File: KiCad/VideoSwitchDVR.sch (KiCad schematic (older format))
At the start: 7 parts, among them SW1 Joystick, U1 ATTINY84-20MU, U2 MAX4624/5

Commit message: Some progress on PCB. MCU changed to simplier one
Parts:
- removed SW1: Joystick, KiCadCustomLibs:5dir6pin10x10mm_Joystick, symbol Joystick
- removed U1: ATTINY84-20MU, Housings_DFN_QFN:UQFN-20-1EP_4x4mm_Pitch0.5mm, symbol ATTINY84-20MU
- added C5: 22uf, Capacitors_SMD:C_0805, symbol C
- added J1: EV100, KiCadCustomLibs:USB_3_PADS, symbol Conn_01x03
- added J2: Buttons, KiCadCustomLibs:USB_3_PADS, symbol Conn_01x03
- added J3: DVR_VIDEO, KiCadCustomLibs:USB_3_PADS, symbol Conn_01x03
- added J4: PWR, KiCadCustomLibs:POWER2PIN, symbol Conn_01x02
- added J5: PWR_DVR, KiCadCustomLibs:POWER2PIN, symbol Conn_01x02
- added J6: PROG, KiCadCustomLibs:Pads_prog_6pin1.25mm, symbol Conn_01x06
- added R1, R2, R3, R4: 100, Resistors_SMD:R_0603, symbol R
- added R5: 10K, Resistors_SMD:R_0603, symbol R
- added U1: ATTINY15-1SC, Housings_SOIC:SOIJ-8_5.3x5.3mm_Pitch1.27mm, symbol ATTINY15-1SC
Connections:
- net labels added: K1, K2, K3, MISO, MOSI, RST, SCK, VID_SENSE, VID_SWITCH
- wire segments 12 -> 37
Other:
- moved on the sheet: C1, C2

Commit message: Some work
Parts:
- removed J2: Buttons, KiCadCustomLibs:USB_3_PADS, symbol Conn_01x03
- added D1: B5819WS, Diodes_SMD:D_SOD-323, symbol D_Schottky
- added J2: Buttons, KiCadCustomLibs:POWER2PIN, symbol Conn_01x02
- added JP1: VCC_SENSE, Resistors_SMD:R_0201_NoSilk, symbol Jumper_NO_Small
- added Q1: AO3415 (P), TO_SOT_Packages_SMD:SOT-23, symbol Q_PMOS_GSD
- added R6: 1K, Resistors_SMD:R_0603, symbol R
- R2: value 100 -> 100K
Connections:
- net K2 is gone; now on net VCC: R2.1
- net MISO: now also R6.1; no longer R2.2
- net VCC: now also D1.1 (K), JP1.2, Q1.2 (S); no longer C5.1, J4.1 (Pin_1), J5.1 (Pin_1)
- net VID_SWITCH: now also U2.1 (IN); no longer U2.5 (COM)
- net at J1.1 (Pin_1): now also U2.5 (COM); no longer U2.1 (IN)
- net K1 renamed B0
- net B0: now also J2.2 (Pin_2), JP1.1
- net K3 renamed B2
- net B2: now also J2.1 (Pin_1)
- new net: D1.2 (A), J4.1 (Pin_1)
- new net: C5.1, J5.1 (Pin_1), Q1.3 (D)
- new net: Q1.1 (G), R2.2, R6.2
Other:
- moved on the sheet: C1, C2, C3, C4, C5, J1, J3, J4, J5, J6, R1, R3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

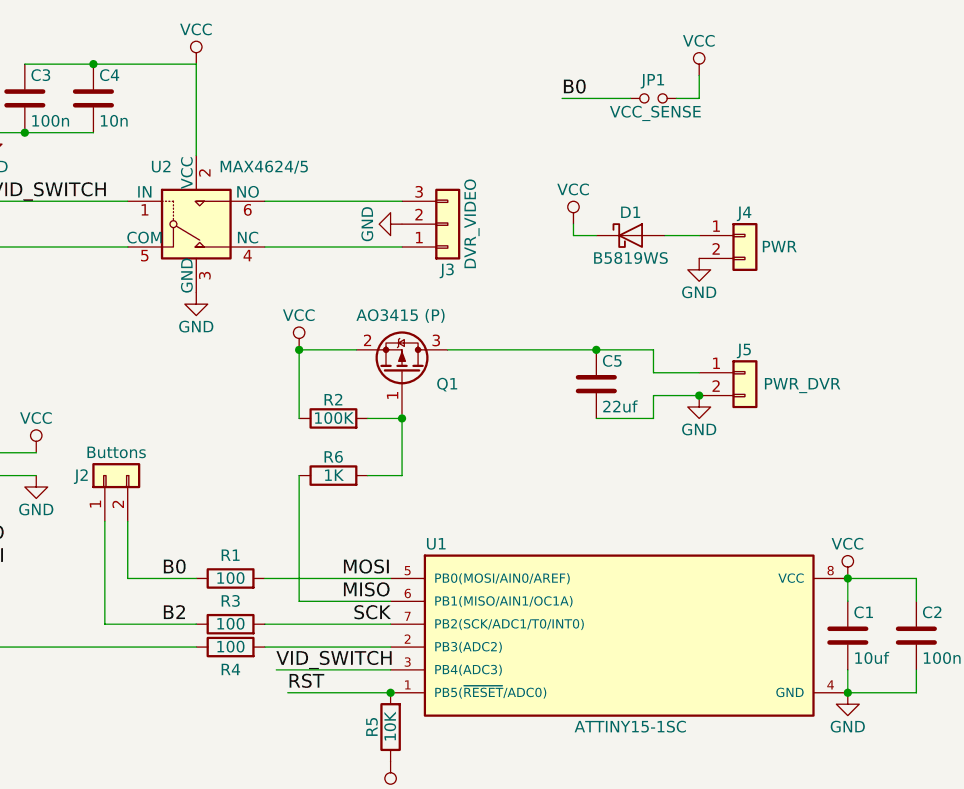
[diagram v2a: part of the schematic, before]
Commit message: Now can use two buttons and power loss sensing at the same time
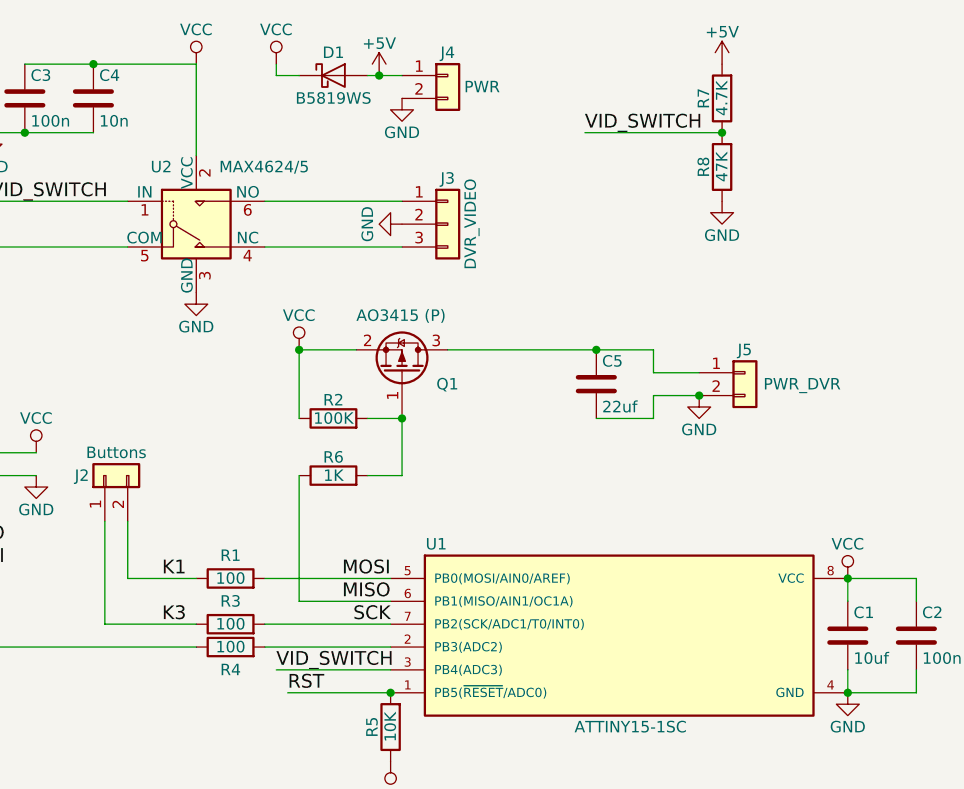
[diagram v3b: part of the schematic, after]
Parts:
- removed JP1: VCC_SENSE, Resistors_SMD:R_0201_NoSilk, symbol Jumper_NO_Small
- added R7: 4.7K, Resistors_SMD:R_0603, symbol R
- added R8: 47K, Resistors_SMD:R_0603, symbol R
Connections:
- net GND: now also R8.1
- net VID_SWITCH: now also R7.1, R8.2
- net at U2.4 (NC): now also J3.3 (Pin_3); no longer J3.1 (Pin_1)
- net at U2.6 (NO): now also J3.1 (Pin_1); no longer J3.3 (Pin_3)
- net +5V: now reaches D1.2 (A), J4.1 (Pin_1)
- net +5V: now also R7.2
- net B0 renamed K1
- net B2 renamed K3
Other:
- moved on the sheet: D1, J4
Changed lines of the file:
@@
 $EndComp
 $Comp
-L VCC #PWR14
+L VCC #PWR16
 U 1 1 5A5D0805
 P 7950 4550
-F 0 "#PWR14" H 7950 4400 50  0001 C CNN
+F 0 "#PWR16" H 7950 4400 50  0001 C CNN
 F 1 "VCC" H 7950 4700 50  0000 C CNN
 F 2 "" H 7950 4550 50  0001 C CNN
@@
 $EndComp
 $Comp
-L GND #PWR15
+L GND #PWR17
 U 1 1 5A5D083A
 P 7950 5050
-F 0 "#PWR15" H 7950 4800 50  0001 C CNN
+F 0 "#PWR17" H 7950 4800 50  0001 C CNN
 F 1 "GND" H 7950 4900 50  0000 C CNN
 F 2 "" H 7950 5050 50  0001 C CNN
@@
 $EndComp
 Text Label 4950 4550 0    60   ~ 0
-B0
+K1
 Text Label 4950 4750 0    60   ~ 0
-B2
+K3
 Text Label 3550 4850 0    60   ~ 0
 VID_SENSE
@@
 $EndComp
 $Comp
-L VCC #PWR8
+L VCC #PWR10
 U 1 1 5A5E0376
 P 5950 5350
-F 0 "#PWR8" H 5950 5200 50  0001 C CNN
+F 0 "#PWR10" H 5950 5200 50  0001 C CNN
 F 1 "VCC" H 5950 5500 50  0000 C CNN
 F 2 "" H 5950 5350 50  0001 C CNN
@@
 F 3 "" H 6200 3000 50  0001 C CNN
 	1    6200 3000
-	1    0    0    1
-$EndComp
-Wire Wire Line
-	6000 3100 5400 3100
-Wire Wire Line
-	5400 2900 6000 2900
-$Comp
-L GND #PWR9
+	1    0    0    -1
+$EndComp
+$Comp
+L GND #PWR12
 U 1 1 5A5E209A
 P 6000 3000
-F 0 "#PWR9" H 6000 2750 50  0001 C CNN
+F 0 "#PWR12" H 6000 2750 50  0001 C CNN
 F 1 "GND" H 6000 2850 50  0000 C CNN
 F 2 "" H 6000 3000 50  0001 C CNN
@@
 L Conn_01x02 J4
 U 1 1 5A5E26FC
-P 7500 3050
-F 0 "J4" H 7500 3150 50  0000 C CNN
-F 1 "PWR" H 7650 3000 50  0000 C CNN
-F 2 "KiCadCustomLibs:POWER2PIN" H 7500 3050 50  0001 C CNN
-F 3 "" H 7500 3050 50  0001 C CNN
-	1    7500 3050
+P 6200 2350
+F 0 "J4" H 6200 2450 50  0000 C CNN
+F 1 "PWR" H 6350 2300 50  0000 C CNN
+F 2 "KiCadCustomLibs:POWER2PIN" H 6200 2350 50  0001 C CNN
+F 3 "" H 6200 2350 50  0001 C CNN
+	1    6200 2350
 	1    0    0    -1
 $EndComp
@@
 $EndComp
 $Comp
-L GND #PWR12
+L GND #PWR11
 U 1 1 5A5E2A7D
-P 7300 3150
-F 0 "#PWR12" H 7300 2900 50  0001 C CNN
-F 1 "GND" H 7300 3000 50  0000 C CNN
-F 2 "" H 7300 3150 50  0001 C CNN
-F 3 "" H 7300 3150 50  0001 C CNN
-	1    7300 3150
+P 6000 2450
+F 0 "#PWR11" H 6000 2200 50  0001 C CNN
+F 1 "GND" H 6000 2300 50  0000 C CNN
+F 2 "" H 6000 2450 50  0001 C CNN
+F 3 "" H 6000 2450 50  0001 C CNN
+	1    6000 2450
 	1    0    0    -1
 $EndComp
@@
 $EndComp
 $Comp
-L VCC #PWR10
+L VCC #PWR7
 U 1 1 5A5E2C27
-P 6750 3000
-F 0 "#PWR10" H 6750 2850 50  0001 C CNN
-F 1 "VCC" H 6750 3150 50  0000 C CNN
-F 2 "" H 6750 3000 50  0001 C CNN
-F 3 "" H 6750 3000 50  0001 C CNN
-	1    6750 3000
-	1    0    0    -1
-$EndComp
-$Comp
-L VCC #PWR7
+P 5450 2300
+F 0 "#PWR7" H 5450 2150 50  0001 C CNN
+F 1 "VCC" H 5450 2450 50  0000 C CNN
+F 2 "" H 5450 2300 50  0001 C CNN
+F 3 "" H 5450 2300 50  0001 C CNN
+	1    5450 2300
+	1    0    0    -1
+$EndComp
+$Comp
+L VCC #PWR8
 U 1 1 5A5E2DA2
 P 5550 3550
-F 0 "#PWR7" H 5550 3400 50  0001 C CNN
+F 0 "#PWR8" H 5550 3400 50  0001 C CNN
 F 1 "VCC" H 5550 3700 50  0000 C CNN
 F 2 "" H 5550 3550 50  0001 C CNN
@@
 L D_Schottky D1
 U 1 1 5AB3C38E
-P 7000 3050
-F 0 "D1" H 7000 3150 50  0000 C CNN
-F 1 "B5819WS" H 7000 2950 50  0000 C CNN
-F 2 "Diodes_SMD:D_SOD-323" H 7000 3050 50  0001 C CNN
-F 3 "" H 7000 3050 50  0001 C CNN
-	1    7000 3050
-	1    0    0    -1
-$EndComp
-Wire Wire Line
-	6750 3000 6750 3050
-Wire Wire Line
-	6750 3050 6850 3050
-Wire Wire Line
-	7150 3050 7300 3050
-$Comp
-L Jumper_NO_Small JP1
-U 1 1 5AB3D25D
-P 7100 2450
-F 0 "JP1" H 7100 2530 50  0000 C CNN
-F 1 "VCC_SENSE" H 7110 2390 50  0000 C CNN
-F 2 "Resistors_SMD:R_0201_NoSilk" H 7100 2450 50  0001 C CNN
-F 3 "" H 7100 2450 50  0001 C CNN
-	1    7100 2450
-	1    0    0    -1
-$EndComp
-$Comp
-L VCC #PWR11
-U 1 1 5AB3D444
-P 7300 2350
-F 0 "#PWR11" H 7300 2200 50  0001 C CNN
-F 1 "VCC" H 7300 2500 50  0000 C CNN
-F 2 "" H 7300 2350 50  0001 C CNN
-F 3 "" H 7300 2350 50  0001 C CNN
-	1    7300 2350
-	1    0    0    -1
-$EndComp
-Wire Wire Line
-	7200 2450 7300 2450
-Wire Wire Line
-	7300 2450 7300 2350
-Wire Wire Line
-	7000 2450 6700 2450
-Text Label 6700 2450 0    60   ~ 0
-B0
+P 5700 2350
+F 0 "D1" H 5700 2450 50  0000 C CNN
+F 1 "B5819WS" H 5700 2250 50  0000 C CNN
+F 2 "Diodes_SMD:D_SOD-323" H 5700 2350 50  0001 C CNN
+F 3 "" H 5700 2350 50  0001 C CNN
+	1    5700 2350
+	1    0    0    -1
+$EndComp
+Wire Wire Line
+	5450 2300 5450 2350
+Wire Wire Line
+	5450 2350 5550 2350
+Wire Wire Line
+	5850 2350 6000 2350
+$Comp
+L +5V #PWR9
+U 1 1 5AB55EBB
+P 5900 2350
+F 0 "#PWR9" H 5900 2200 50  0001 C CNN
+F 1 "+5V" H 5900 2490 50  0000 C CNN
+F 2 "" H 5900 2350 50  0001 C CNN
+F 3 "" H 5900 2350 50  0001 C CNN
+	1    5900 2350
+	1    0    0    -1
+$EndComp
+Connection ~ 5900 2350
+$Comp
+L R R7
+U 1 1 5AB56263
+P 7400 2450
+F 0 "R7" V 7480 2450 50  0000 C CNN
+F 1 "4.7K" V 7400 2450 50  0000 C CNN
+F 2 "Resistors_SMD:R_0603" V 7330 2450 50  0001 C CNN
+F 3 "" H 7400 2450 50  0001 C CNN
+	1    7400 2450
+	-1   0    0    1
+$EndComp
+$Comp
+L R R8
+U 1 1 5AB565FD
+P 7400 2750
+F 0 "R8" V 7480 2750 50  0000 C CNN
+F 1 "47K" V 7400 2750 50  0000 C CNN
+F 2 "Resistors_SMD:R_0603" V 7330 2750 50  0001 C CNN
+F 3 "" H 7400 2750 50  0001 C CNN
+	1    7400 2750
+	-1   0    0    1
+$EndComp
+Wire Wire Line
+	7400 2600 6800 2600
+Text Label 6800 2600 0    60   ~ 0
+VID_SWITCH
+Connection ~ 7400 2600
+$Comp
+L +5V #PWR14
+U 1 1 5AB56ADA
+P 7400 2300
+F 0 "#PWR14" H 7400 2150 50  0001 C CNN
+F 1 "+5V" H 7400 2440 50  0000 C CNN
+F 2 "" H 7400 2300 50  0001 C CNN
+F 3 "" H 7400 2300 50  0001 C CNN
+	1    7400 2300
+	1    0    0    -1
+$EndComp
+$Comp
+L GND #PWR15
+U 1 1 5AB56B5D
+P 7400 2900
+F 0 "#PWR15" H 7400 2650 50  0001 C CNN
+F 1 "GND" H 7400 2750 50  0000 C CNN
+F 2 "" H 7400 2900 50  0001 C CNN
+F 3 "" H 7400 2900 50  0001 C CNN
+	1    7400 2900
+	1    0    0    -1
+$EndComp
+Wire Wire Line
+	6000 2900 5400 2900
+Wire Wire Line
+	5400 3100 6000 3100
 $EndSCHEMATC

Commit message: alfa version is 90% tested
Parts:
- U1: value ATTINY15-1SC -> ATTINY25
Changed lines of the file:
@@
 P 6950 4800
 F 0 "U1" H 6150 5200 50  0000 C CNN
-F 1 "ATTINY15-1SC" H 7000 4400 50  0000 C CNN
+F 1 "ATTINY25" H 7000 4400 50  0000 C CNN
 F 2 "Housings_SOIC:SOIJ-8_5.3x5.3mm_Pitch1.27mm" H 7550 4800 50  0001 C CIN
 F 3 "" H 6150 5150 50  0001 C CNN

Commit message: PCB 2.0. Case SCAD.
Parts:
- removed R1, R3: 100, Resistors_SMD:R_0603, symbol R
- removed R5: 10K, Resistors_SMD:R_0603, symbol R
- added J7: SuperCap, KiCadCustomLibs:ESC_PWR_PAD, symbol Conn_01x01
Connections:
- net K1 is gone; now on net MOSI: J2.2 (Pin_2)
- net K3 is gone; now on net SCK: J2.1 (Pin_1)
- net VCC: now also J7.1 (Pin_1)
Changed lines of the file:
@@
 	1    0    0    -1
 $EndComp
-Text Label 4950 4550 0    60   ~ 0
-K1
-Text Label 4950 4750 0    60   ~ 0
-K3
 Text Label 3550 4850 0    60   ~ 0
 VID_SENSE
@@
 Wire Wire Line
 	8250 5050 8250 4950
-$Comp
-L R R5
-U 1 1 5A5E024F
-P 5950 5200
-F 0 "R5" V 6030 5200 50  0000 C CNN
-F 1 "10K" V 5950 5200 50  0000 C CNN
-F 2 "Resistors_SMD:R_0603" V 5880 5200 50  0001 C CNN
-F 3 "" H 5950 5200 50  0001 C CNN
-	1    5950 5200
-	-1   0    0    1
-$EndComp
-$Comp
-L VCC #PWR10
-U 1 1 5A5E0376
-P 5950 5350
-F 0 "#PWR10" H 5950 5200 50  0001 C CNN
-F 1 "VCC" H 5950 5500 50  0000 C CNN
-F 2 "" H 5950 5350 50  0001 C CNN
-F 3 "" H 5950 5350 50  0001 C CNN
-	1    5950 5350
-	-1   0    0    1
-$EndComp
-$Comp
-L R R1
-U 1 1 5A5E06DD
-P 5250 4550
-F 0 "R1" V 5350 4550 50  0000 C CNN
-F 1 "100" V 5250 4550 50  0000 C CNN
-F 2 "Resistors_SMD:R_0603" V 5180 4550 50  0001 C CNN
-F 3 "" H 5250 4550 50  0001 C CNN
-	1    5250 4550
-	0    -1   -1   0
-$EndComp
-$Comp
-L R R3
-U 1 1 5A5E0924
-P 5250 4750
-F 0 "R3" V 5350 4750 50  0000 C CNN
-F 1 "100" V 5250 4750 50  0000 C CNN
-F 2 "Resistors_SMD:R_0603" V 5180 4750 50  0001 C CNN
-F 3 "" H 5250 4750 50  0001 C CNN
-	1    5250 4750
-	0    -1   -1   0
-$EndComp
-Wire Wire Line
-	5400 4550 5950 4550
+Wire Wire Line
+	4800 4550 5950 4550
 Wire Wire Line
 	5550 4650 5950 4650
 Wire Wire Line
-	5400 4750 5950 4750
-Wire Wire Line
-	4800 4550 5100 4550
-Wire Wire Line
-	4700 4750 5100 4750
+	4700 4750 5950 4750
 $Comp
 L R R4
@@
 $EndComp
 $Comp
-L GND #PWR12
+L GND #PWR11
 U 1 1 5A5E209A
 P 6000 3000
-F 0 "#PWR12" H 6000 2750 50  0001 C CNN
+F 0 "#PWR11" H 6000 2750 50  0001 C CNN
 F 1 "GND" H 6000 2850 50  0000 C CNN
 F 2 "" H 6000 3000 50  0001 C CNN
@@
 $EndComp
 $Comp
-L GND #PWR11
+L GND #PWR10
 U 1 1 5A5E2A7D
 P 6000 2450
-F 0 "#PWR11" H 6000 2200 50  0001 C CNN
+F 0 "#PWR10" H 6000 2200 50  0001 C CNN
 F 1 "GND" H 6000 2300 50  0000 C CNN
 F 2 "" H 6000 2450 50  0001 C CNN
@@
 Connection ~ 5550 3550
 Connection ~ 6850 3550
-Connection ~ 5950 5050
 $Comp
 L Conn_01x02 J2
@@
 Wire Wire Line
 	5400 3100 6000 3100
+$Comp
+L Conn_01x01 J7
+U 1 1 5AEB1E50
+P 7500 3250
+F 0 "J7" H 7500 3350 50  0000 C CNN
+F 1 "SuperCap" H 7500 3150 50  0000 C CNN
+F 2 "KiCadCustomLibs:ESC_PWR_PAD" H 7500 3250 50  0001 C CNN
+F 3 "" H 7500 3250 50  0001 C CNN
+	1    7500 3250
+	1    0    0    -1
+$EndComp
+$Comp
+L VCC #PWR12
+U 1 1 5AEB1EFA
+P 7150 3250
+F 0 "#PWR12" H 7150 3100 50  0001 C CNN
+F 1 "VCC" H 7150 3400 50  0000 C CNN
+F 2 "" H 7150 3250 50  0001 C CNN
+F 3 "" H 7150 3250 50  0001 C CNN
+	1    7150 3250
+	1    0    0    -1
+$EndComp
+Wire Wire Line
+	7150 3250 7300 3250
 $EndSCHEMATC
